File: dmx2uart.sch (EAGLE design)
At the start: 6 parts, among them IC1 MAX487

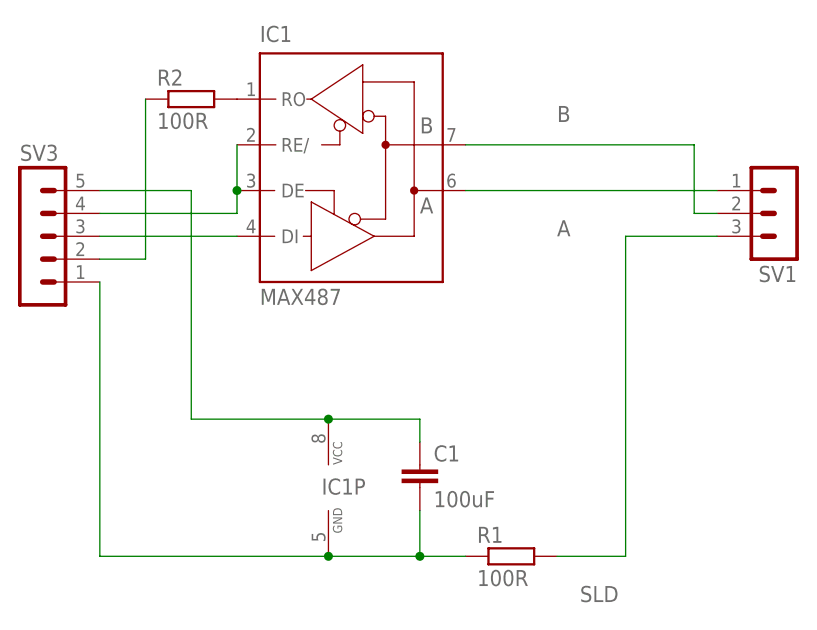
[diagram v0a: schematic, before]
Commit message: capacitor size
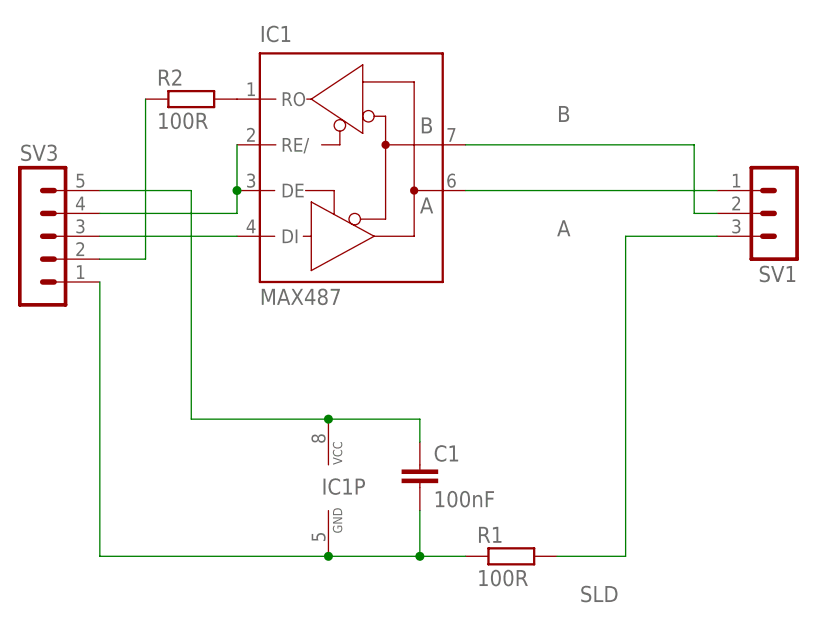
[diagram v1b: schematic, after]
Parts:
- C1: value 100uF -> 100nF
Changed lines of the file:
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@@
 <parts>
 <part name="IC1" library="maxim" deviceset="MAX481CPA" device="" value="MAX487"/>
-<part name="C1" library="rcl" deviceset="C-EU" device="075-032X103" value="100uF"/>
+<part name="C1" library="rcl" deviceset="C-EU" device="075-032X103" value="100nF"/>
 <part name="R1" library="rcl" deviceset="R-EU_" device="0207/7" value="100R"/>
 <part name="R2" library="resistor" deviceset="R-EU_" device="0207/10" value="100R"/>
